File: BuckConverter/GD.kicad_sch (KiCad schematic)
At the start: 18 parts, among them U3 UCC5304DWVR, U4 TMV 0512SHI

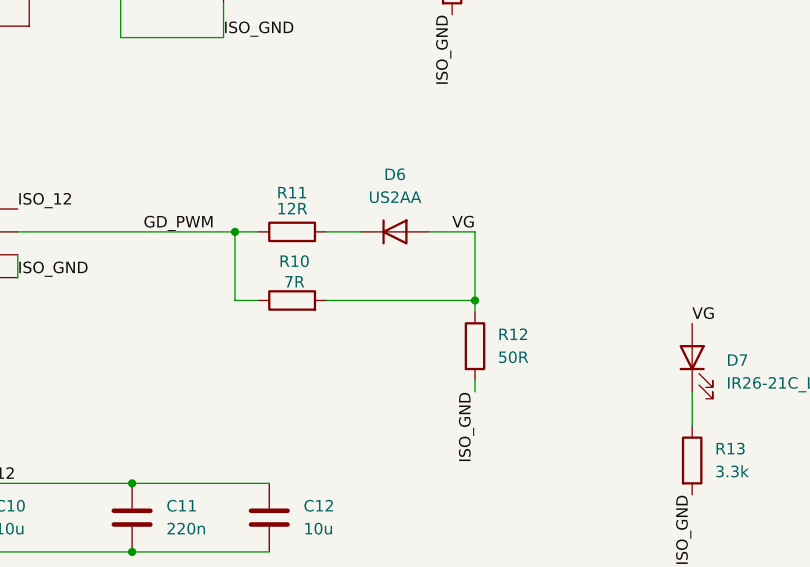
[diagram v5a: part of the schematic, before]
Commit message: added BOM cvs
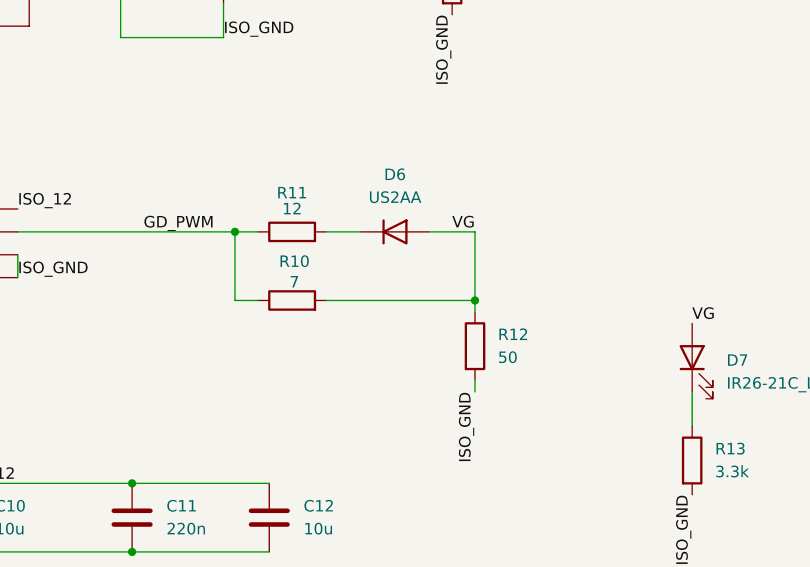
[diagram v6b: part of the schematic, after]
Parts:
- R10: value 7R -> 7; Part Number RMCF0805FT10K0 -> CRCW08057R15FKEA
- R11: value 12R -> 12
- R12: value 50R -> 50
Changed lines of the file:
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@@
 			)
 		)
-		(property "Value" "12R"
+		(property "Value" "12"
 			(at 171.45 80.01 90)
 			(effects
@@
 			)
 		)
-		(property "Value" "7R"
+		(property "Value" "7"
 			(at 171.704 88.138 90)
 			(effects
@@
 			)
 		)
-		(property "Part Number" "RMCF0805FT10K0"
+		(property "Part Number" "CRCW08057R15FKEA"
 			(at 171.45 90.17 0)
 			(effects
@@
 			)
 		)
-		(property "Value" "50R"
+		(property "Value" "50"
 			(at 194.31 96.5199 0)
 			(effects
